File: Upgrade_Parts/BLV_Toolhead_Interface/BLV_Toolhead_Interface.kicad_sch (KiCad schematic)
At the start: 22 parts, among them J1 RB1-125B8G1A, J2 Micro-Fit, J3 JST-3, J4 JST-4, J5 Screw Terminal, J6 JST-5, U1 SN65LVDS1, U2 SN65LVDS2, U3 SN65LVDS2

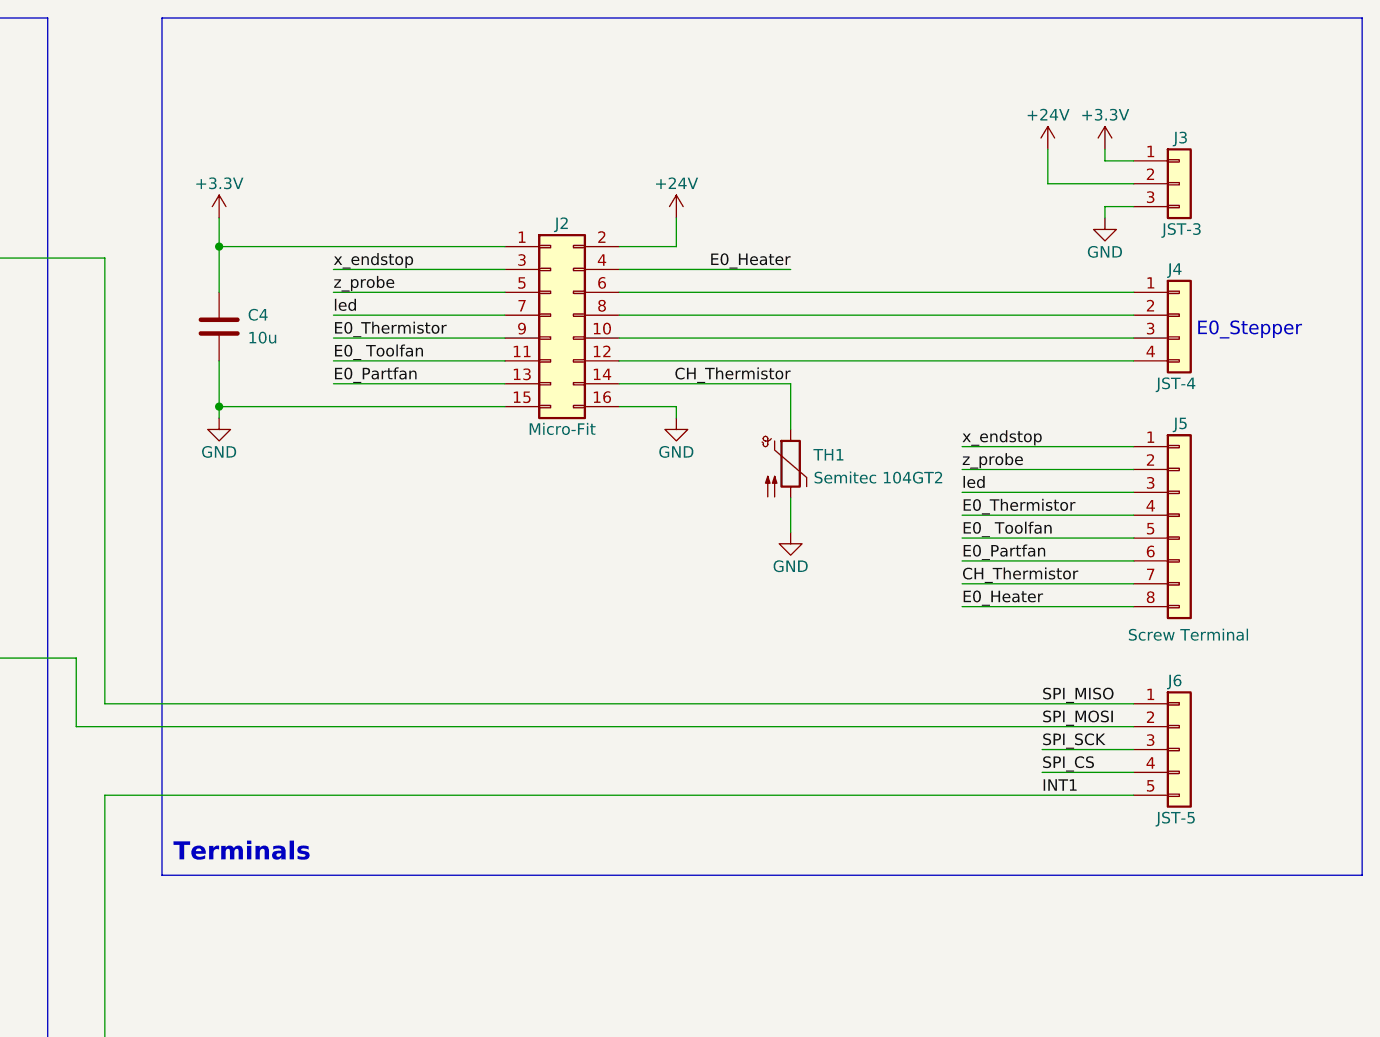
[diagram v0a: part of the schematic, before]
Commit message: added terminals
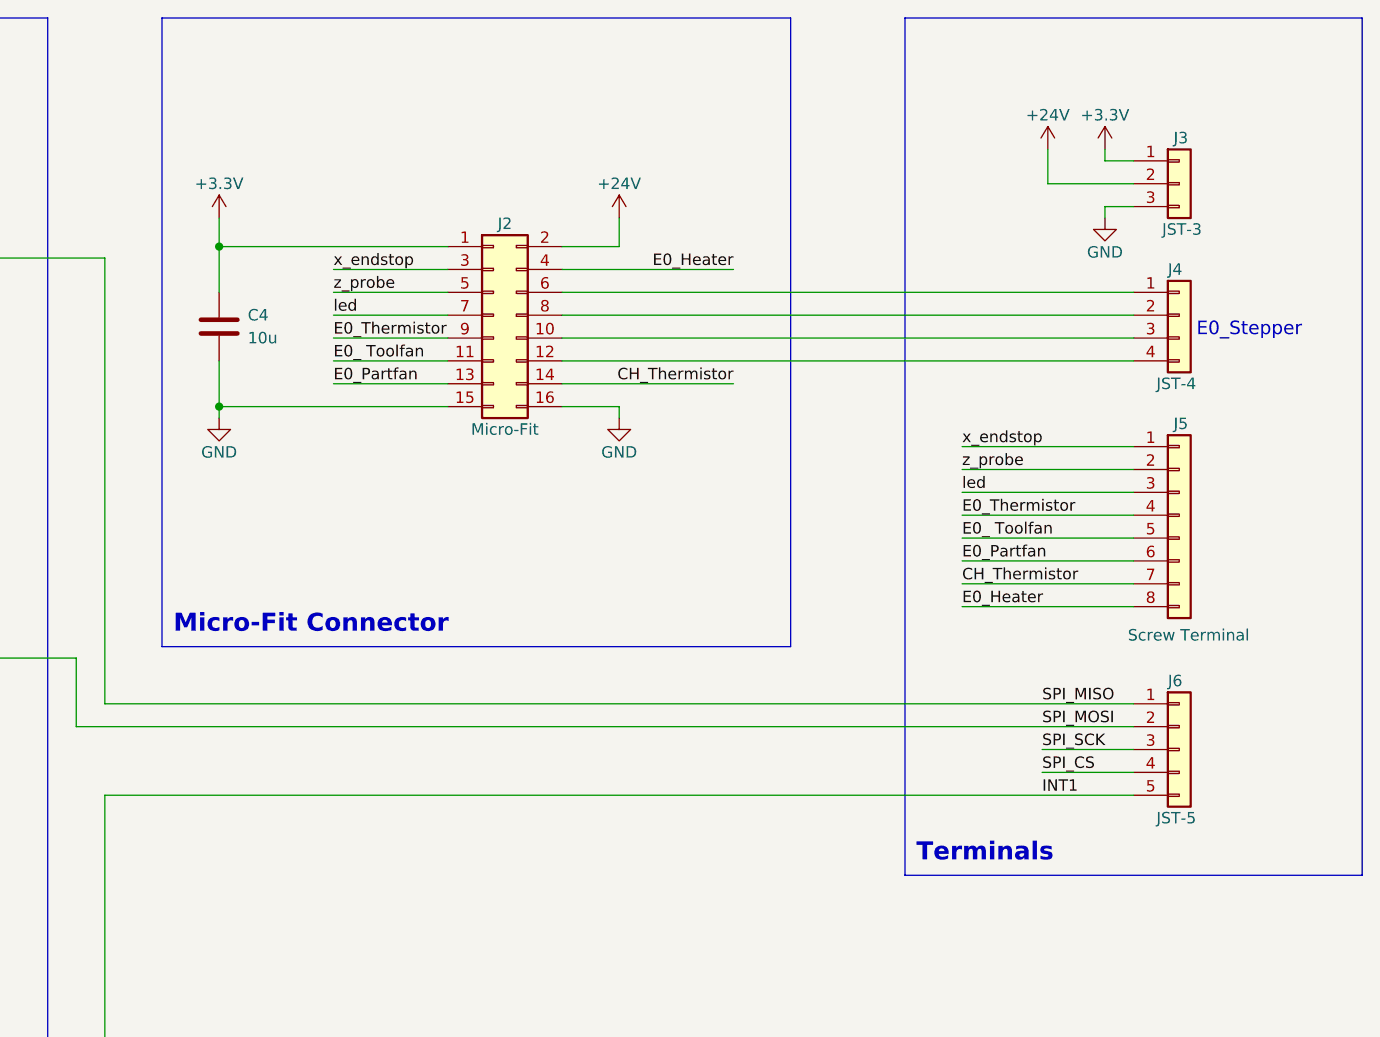
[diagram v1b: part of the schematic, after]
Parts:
- removed TH1: Semitec 104GT2, Resistor_THT:R_Axial_DIN0207_L6.3mm_D2.5mm_P10.16mm_Horizontal, symbol Device:Thermistor_PTC
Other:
- note added: "Micro-Fit Connector"
- company: (none) -> https://github.com/Battosai42/CraftbotPlus_Upgrade
- title: (none) -> BLV Toolheat Interface Board
- moved on the sheet: J2
